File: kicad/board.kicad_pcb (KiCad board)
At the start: 2 copper layers, 154.2 x 107.9 mm, 58 parts

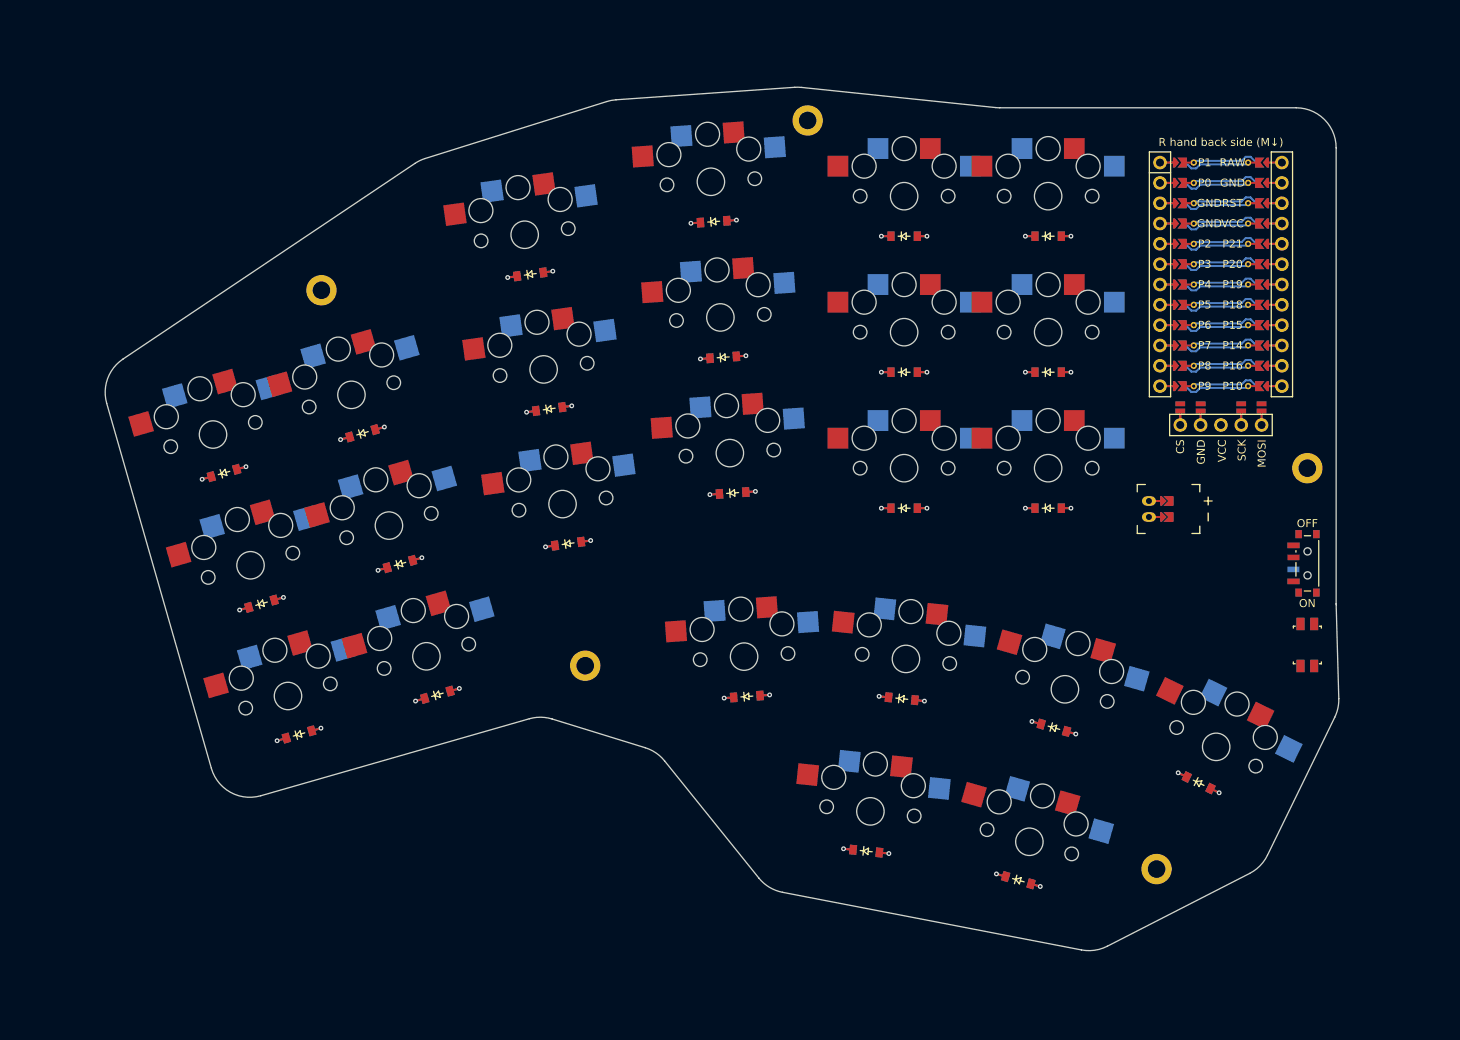
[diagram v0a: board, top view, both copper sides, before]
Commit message: realizing I'm going to want to change some of the layout
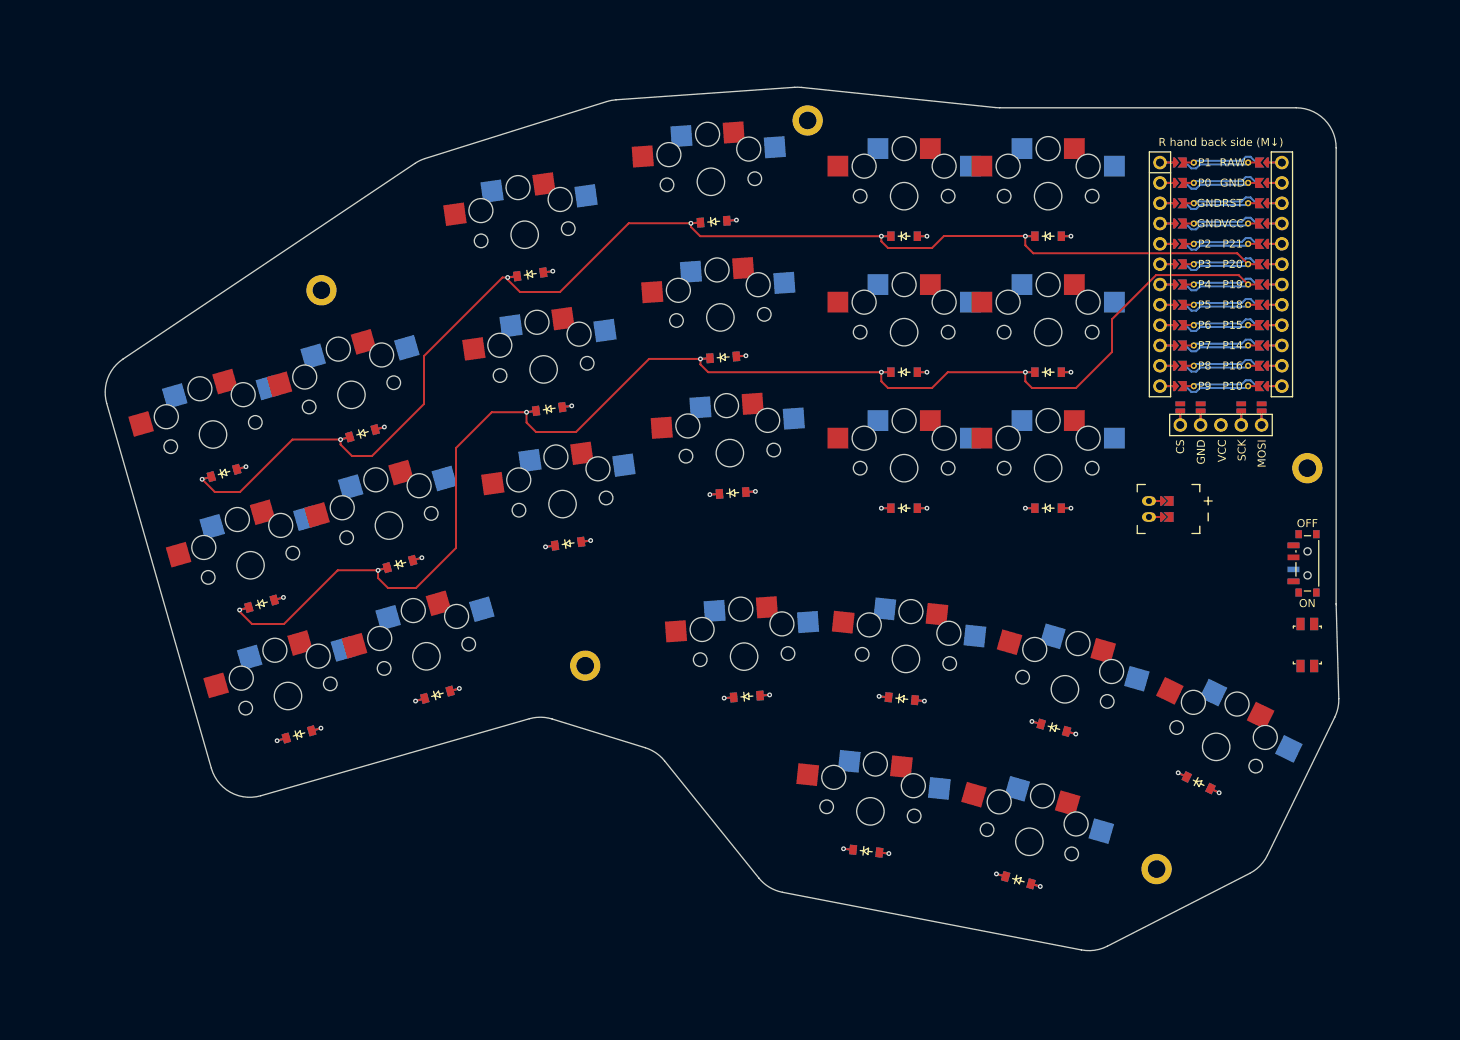
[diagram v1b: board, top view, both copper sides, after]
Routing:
- net (no net): track 337.7 -> 0.00 mm
- net P19: track 14.4 -> 191.0 mm
- net P20: track 14.4 -> 181.5 mm
- net GND: track 0.00 -> 29.5 mm
- net P9: track 0.00 -> 9.84 mm
- net P4: track 0.00 -> 9.84 mm
- net P2: track 0.00 -> 9.84 mm
- net SCK: track 0.00 -> 9.84 mm
- net P8: track 0.00 -> 9.84 mm
- net P3: track 0.00 -> 9.84 mm
- net P1: track 0.00 -> 9.84 mm
- net P0: track 0.00 -> 9.84 mm
- net MOSI: track 0.00 -> 9.84 mm
- net CS: track 0.00 -> 9.84 mm
- net P21: track 14.4 -> 24.2 mm
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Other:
- net class Default removed

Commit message: rebased and pulled in new footprints
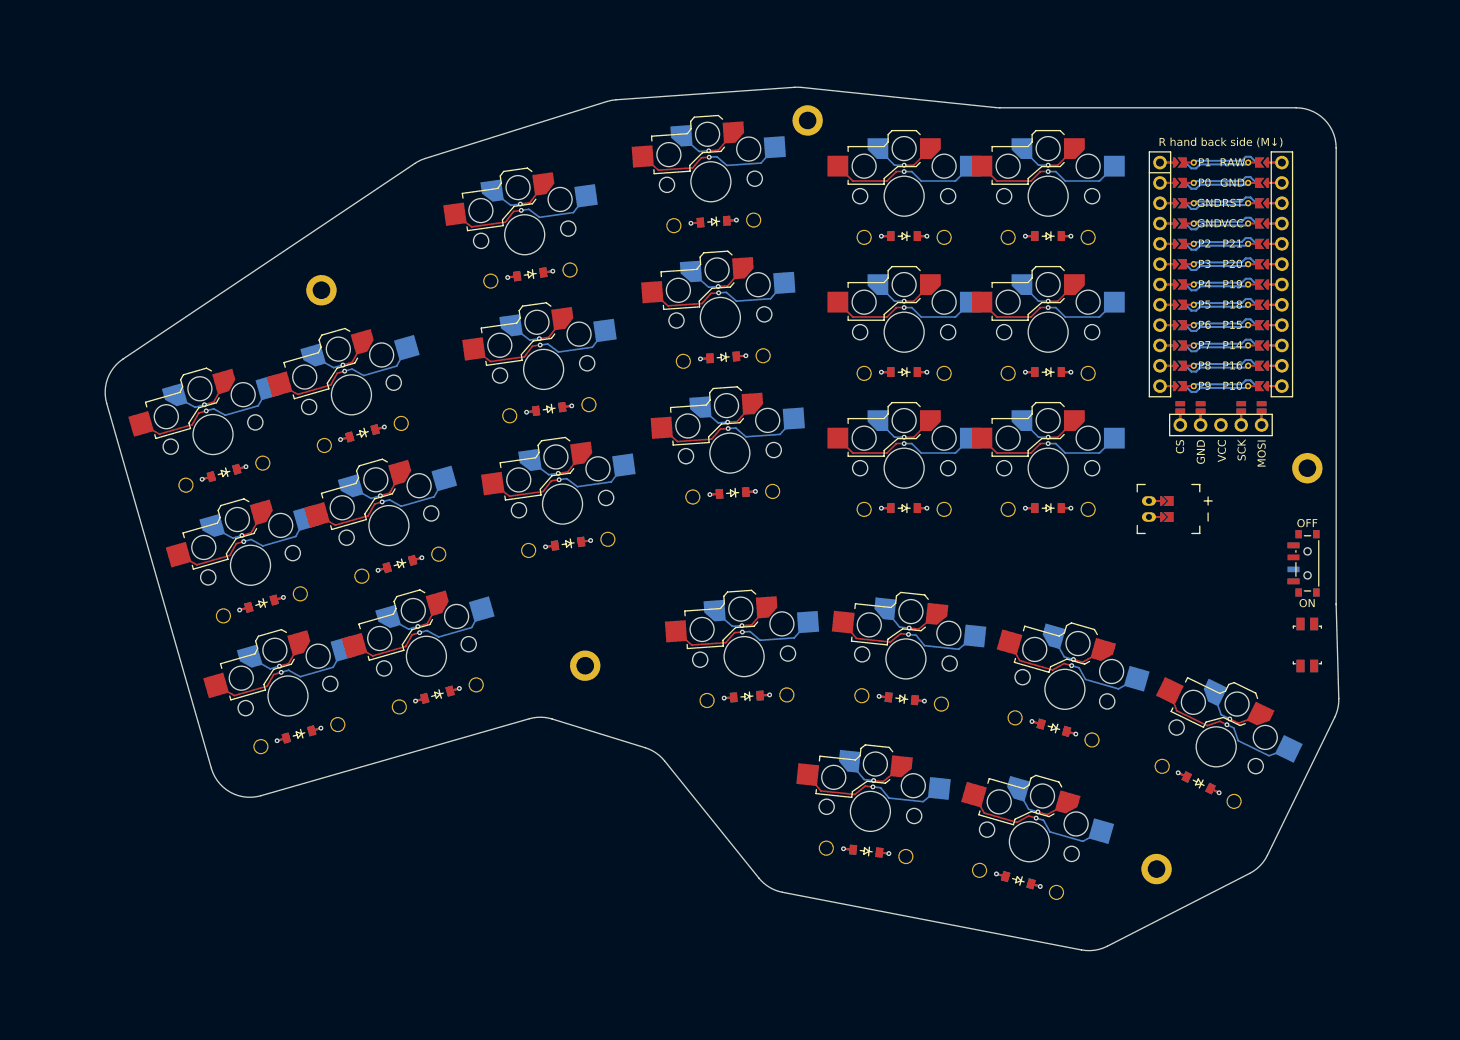
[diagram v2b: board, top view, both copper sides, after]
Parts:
- S1, S10, S11, S12, S13, S14, S15, S16, S17, S18, S19, S2, S20, S21, S22, S23, S24, S3, S4, S5, S6, S7, S8, S9: footprint PG1350 -> ceoloide:switch_choc_v1_v2; moved to B.Cu
- turned D24 to 164 degrees
- turned D6 to 196 degrees
- turned D21 to 164 degrees
- turned D1 to 196 degrees
- turned D10 to 184 degrees
- turned D9 to 188 degrees
- turned D13 to 180 degrees
- turned D14 to 180 degrees
- turned D15 to 180 degrees
- turned D5 to 196 degrees
- turned D20 to 174 degrees
- turned D7 to 188 degrees
- turned D11 to 184 degrees
- turned D23 to 174 degrees
- turned D16 to 180 degrees
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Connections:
- D1 pad 1: P18 -> P19
- D10 pad 1: P18 -> P19
- D11 pad 1: P19 -> P20
- D12 pad 1: P20 -> P21
- D13 pad 1: P18 -> P19
- D14 pad 1: P19 -> P20
- D15 pad 1: P20 -> P21
- D16 pad 1: P18 -> P19
- D17 pad 1: P19 -> P20
- D18 pad 1: P20 -> P21
- D19 pad 1: P21 -> P18
- D2 pad 1: P19 -> P20
- D20 pad 1: P21 -> P18
- D21 pad 1: P21 -> P18
- D22 pad 1: P21 -> P18
- D23 pad 1: P21 -> P18
- D24 pad 1: P21 -> P18
- D3 pad 1: P20 -> P21
- D4 pad 1: P18 -> P19
- D5 pad 1: P19 -> P20
- D6 pad 1: P20 -> P21
- D7 pad 1: P18 -> P19
- D8 pad 1: P19 -> P20
- D9 pad 1: P20 -> P21
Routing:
- net (no net): track 0.00 -> 337.7 mm
- net P19: track 191.0 -> 14.4 mm
- net P20: track 181.5 -> 14.4 mm
- net GND: track 29.5 -> 0.00 mm
- net P10: track 9.83 -> 33.1 mm, vias 0 -> 4
- net P15: track 9.83 -> 33.1 mm, vias 0 -> 4
- net P16: track 9.83 -> 33.1 mm, vias 0 -> 4
- net P14: track 9.83 -> 33.1 mm, vias 0 -> 4
- net P8: track 9.84 -> 33.1 mm, vias 0 -> 4
- net P9: track 9.84 -> 33.1 mm, vias 0 -> 4
- net middle_top: track 2.40 -> 21.5 mm, vias 1 -> 2
- net tb_outer_tb_bot: track 2.40 -> 21.5 mm, vias 1 -> 2
- net tt_middle_tt_top: track 2.40 -> 21.5 mm, vias 1 -> 2
- net inner_top: track 2.40 -> 21.5 mm, vias 1 -> 2
- net inner_home: track 2.40 -> 21.5 mm, vias 1 -> 2
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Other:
- net class Default added: clearance 0.2, trace_width 0.25, via_dia 0.8, via_drill 0.4

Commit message: routing coming along nicely
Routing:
- net (no net): track 337.7 -> 0.00 mm
- net P18: track 14.4 -> 206.6 mm
- net P19: track 14.4 -> 186.7 mm
- net P21: track 14.4 -> 171.6 mm
- net P20: track 14.4 -> 159.3 mm
- net RST: track 0.00 -> 76.0 mm
- net RAW: track 0.00 -> 65.4 mm
- net BAT_P: track 0.00 -> 46.0 mm
- net GND: track 0.00 -> 29.5 mm
- net MOSI: track 0.00 -> 27.6 mm
- net SCK: track 0.00 -> 23.4 mm
- net CS: track 0.00 -> 19.0 mm
- net P9: track 33.1 -> 42.9 mm
- net P4: track 0.00 -> 9.84 mm
- net P2: track 0.00 -> 9.84 mm
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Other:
- net class Default removed

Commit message: just need to zone fill
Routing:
- net P8: track 42.9 -> 263.3 mm, vias 4 -> 7
- net P14: track 42.9 -> 217.5 mm, vias 4 -> 7
- net P9: track 42.9 -> 198.4 mm, vias 4 -> 7
- net P10: track 42.9 -> 191.5 mm, vias 4 -> 6
- net P15: track 42.9 -> 176.5 mm
- net P16: track 42.9 -> 153.7 mm
- net RST: track 76.0 -> 141.2 mm
- net RAW: track 65.4 -> 123.3 mm
- net BAT_P: track 46.0 -> 103.8 mm
- net MOSI: track 27.6 -> 66.6 mm
- net SCK: track 23.4 -> 55.8 mm
- net CS: track 19.0 -> 34.7 mm
- net tb_outer_tb_bot: track 28.4 -> 32.6 mm
- net tt_middle_tt_top: track 28.4 -> 32.6 mm
- net tt_inner_tt_top: track 28.9 -> 32.9 mm
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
